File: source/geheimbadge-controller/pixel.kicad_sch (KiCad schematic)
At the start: 2 parts

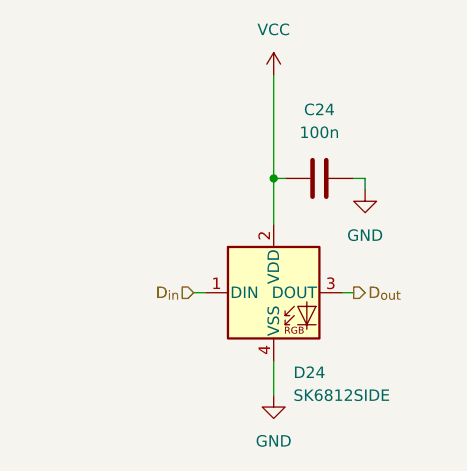
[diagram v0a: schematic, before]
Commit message: new led orientation; no signal resistors
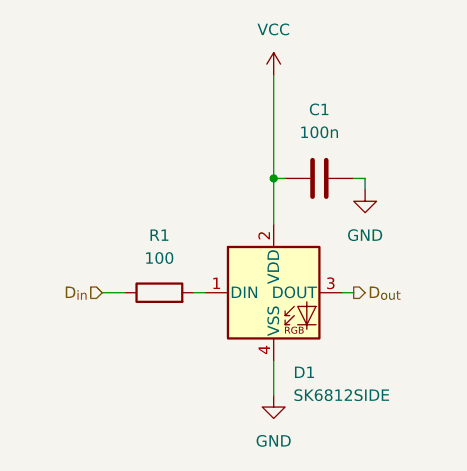
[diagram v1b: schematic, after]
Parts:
- added R1: 100, Resistor_SMD:R_0402_1005Metric, symbol Device:R
- renumbered C24 to C1, D24 to D1
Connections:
- net D_{in}: now also R1.1; no longer D1.1 (DIN)
- new net: D1.1 (DIN), R1.2
